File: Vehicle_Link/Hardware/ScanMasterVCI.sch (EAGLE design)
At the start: 86 parts, among them IC1 XMEGA32A4U, IC2 TL331, P1 HARFLEX-1515012-601, Q1 RUM002N05, Q10 ZXMP6A17G, Q3 RUM002N05, Q4 RUM002N05, Q5 RRF015P03, Q6 RUM002N05, Q7 RRF015P03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

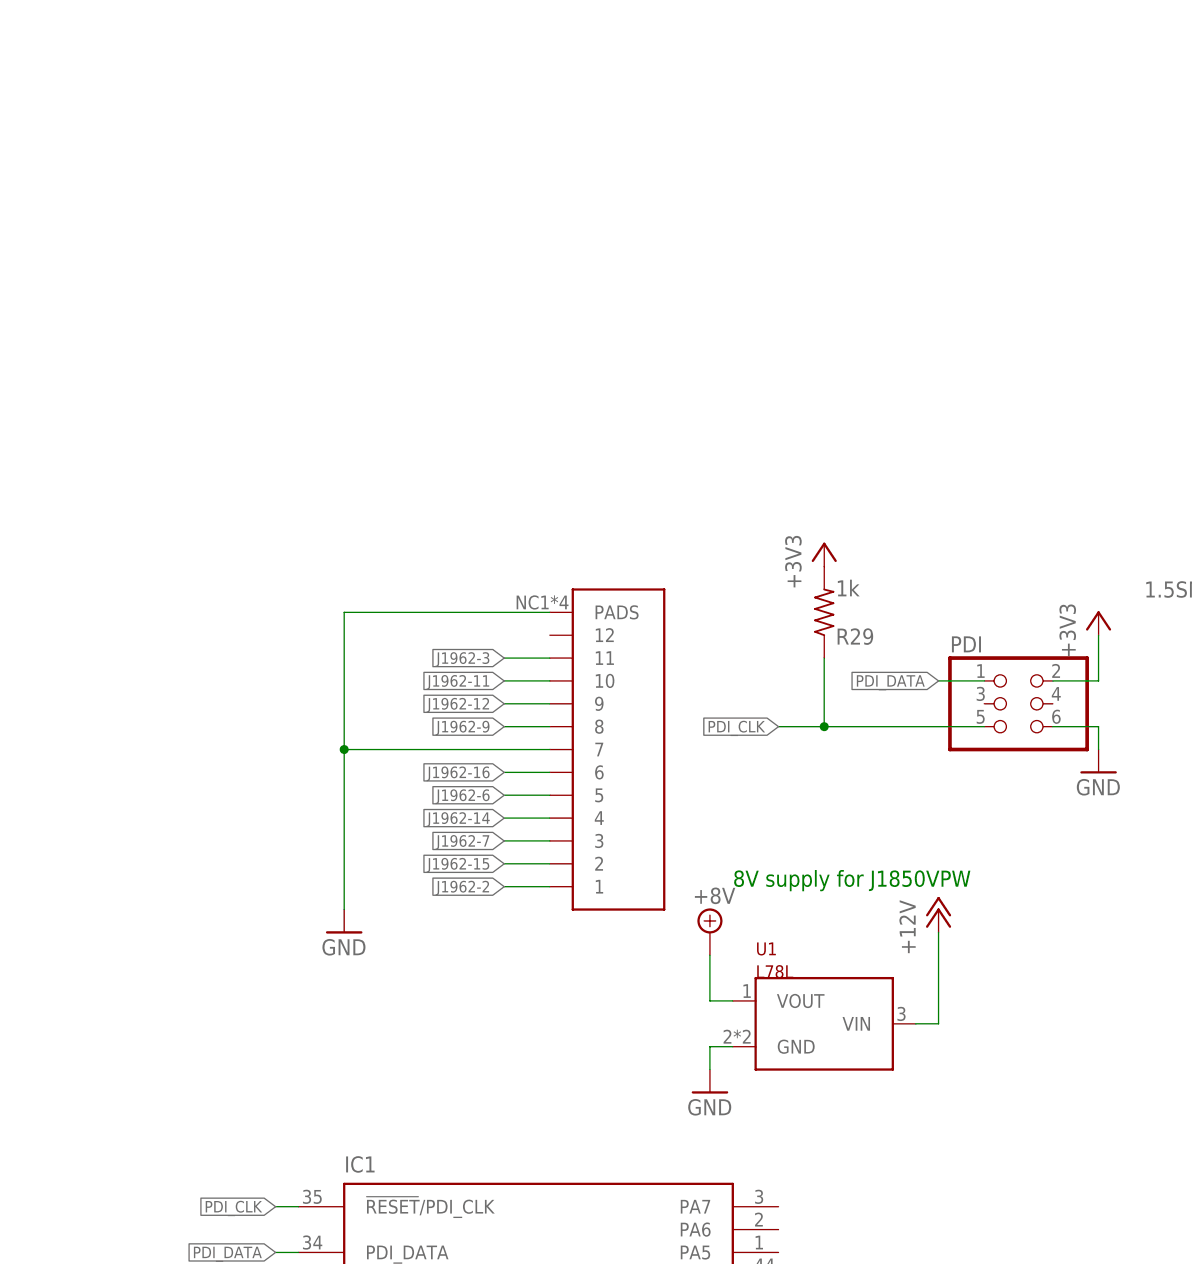
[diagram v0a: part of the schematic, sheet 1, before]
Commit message: Added OBD connector board section, along with proper connectors so I don't have to solder wires anymore. Still need to add milling marks
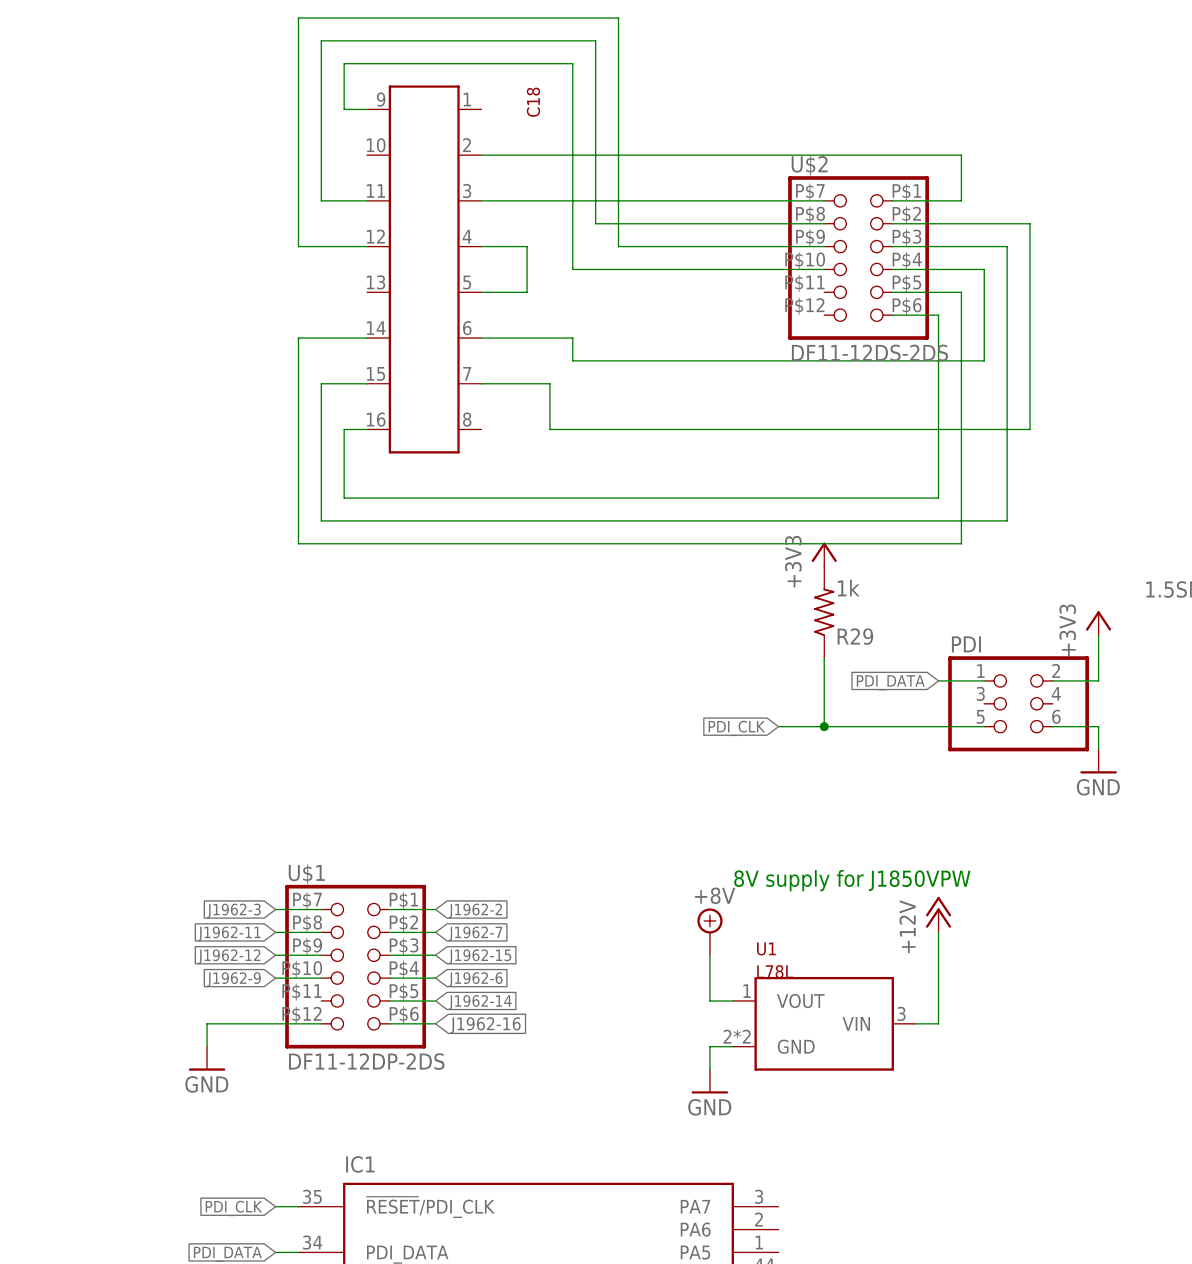
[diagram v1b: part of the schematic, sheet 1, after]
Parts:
- removed P1: HARFLEX-1515012-601, customics:HARFLEX-1515012-601
- added C18: J1962M, customics:J1962M
- added U$1: DF11-12DP-2DS, customics:DF11-12DP-2DS
- added U$2: DF11-12DS-2DS, customics:DF11-12DS-2DS
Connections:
- new net N$14: C18.16, U$2.6
- new net N$25: C18.15, U$2.3
- new net N$28: C18.14, U$2.5
- new net N$29: C18.6, U$2.4
- new net N$32: C18.7, U$2.2
- new net N$40: C18.4, C18.5
- new net N$41: C18.3, U$2.7
- new net N$42: C18.9, U$2.10
- new net N$43: C18.12, U$2.9
- new net N$44: C18.11, U$2.8
- new net N$46: C18.2, U$2.1
- net GND: now also U$1.12; no longer P1.7, P1.PADS
- net J1962-11: now also U$1.8; no longer P1.10
- net J1962-12: now also U$1.9; no longer P1.9
- net J1962-14: now also U$1.5; no longer P1.4
- net J1962-15: now also U$1.3; no longer P1.2
- net J1962-16: now also U$1.6; no longer P1.6
- net J1962-2: now also U$1.1; no longer P1.1
- net J1962-3: now also U$1.7; no longer P1.11
- net J1962-6: now also U$1.4; no longer P1.5
- net J1962-7: now also U$1.2; no longer P1.3
- net J1962-9: now also U$1.10; no longer P1.8

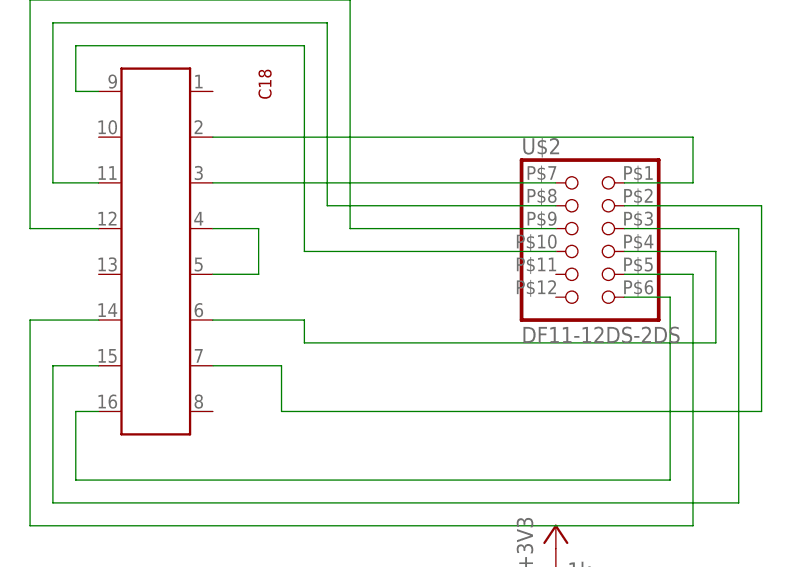
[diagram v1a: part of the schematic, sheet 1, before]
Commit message: Finished adding milling marks to the OBD connector PCB. Missed a ground connection on the OBD board, added it.
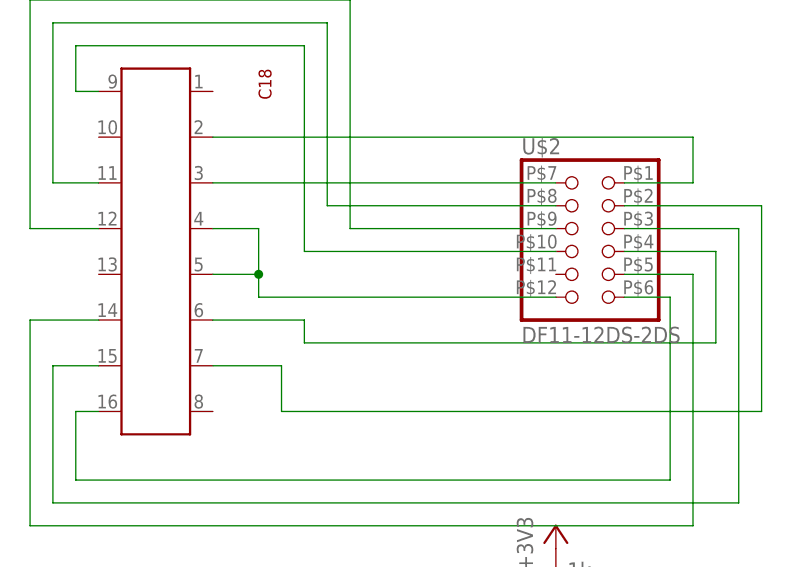
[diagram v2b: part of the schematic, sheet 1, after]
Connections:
- net N$14 renamed CVBATT
- removed net N$40: C18.4, C18.5
- new net CGND: C18.4, C18.5, U$2.12
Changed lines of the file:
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@@
 </segment>
 </net>
-<net name="N$14" class="0">
+<net name="CVBATT" class="1">
 <segment>
 <wire x1="88.9" y1="187.96" x2="88.9" y2="167.64" width="0.1524" layer="91"/>
@@
 </segment>
 </net>
-<net name="N$40" class="0">
+<net name="CGND" class="1">
 <segment>
 <pinref part="C18" gate="G$1" pin="5"/>
@@
 <wire x1="38.1" y1="195.58" x2="43.18" y2="195.58" width="0.1524" layer="91"/>
 <wire x1="43.18" y1="195.58" x2="43.18" y2="190.5" width="0.1524" layer="91"/>
+<wire x1="43.18" y1="190.5" x2="43.18" y2="187.96" width="0.1524" layer="91"/>
+<junction x="43.18" y="190.5"/>
+<pinref part="U$2" gate="G$1" pin="12"/>
+<wire x1="43.18" y1="187.96" x2="76.2" y2="187.96" width="0.1524" layer="91"/>
 </segment>
 </net>

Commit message: Switched XMEGA to the 44QFN variety. Changed the OBD connection, expanded the size of the board just a little to accomodate the new connector.
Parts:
- removed C18: J1962M, customics:J1962M
- removed U$1: DF11-12DP-2DS, customics:DF11-12DP-2DS
- removed U$2: DF11-12DS-2DS, customics:DF11-12DS-2DS
- added OBD1: (no value), customics:OBD2_OBD2_90
- IC1: device atmel:XMEGA16A4A -> atmel:XMEGA16A4M1
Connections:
- removed net CGND: C18.4, C18.5, U$2.12
- removed net CVBATT: C18.16, U$2.6
- removed net N$25: C18.15, U$2.3
- removed net N$28: C18.14, U$2.5
- removed net N$29: C18.6, U$2.4
- removed net N$32: C18.7, U$2.2
- removed net N$41: C18.3, U$2.7
- removed net N$42: C18.9, U$2.10
- removed net N$43: C18.12, U$2.9
- removed net N$44: C18.11, U$2.8
- removed net N$46: C18.2, U$2.1
- net GND: now also OBD1.4, OBD1.5; no longer U$1.12
- net J1962-11: now also OBD1.11; no longer U$1.8
- net J1962-12: now also OBD1.12; no longer U$1.9
- net J1962-14: now also OBD1.14; no longer U$1.5
- net J1962-15: now also OBD1.15; no longer U$1.3
- net J1962-16: now also OBD1.16; no longer U$1.6
- net J1962-2: now also OBD1.2; no longer U$1.1
- net J1962-3: now also OBD1.3; no longer U$1.7
- net J1962-6: now also OBD1.6; no longer U$1.4
- net J1962-7: now also OBD1.7; no longer U$1.2
- net J1962-9: now also OBD1.9; no longer U$1.10
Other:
- moved on the sheet: U3A

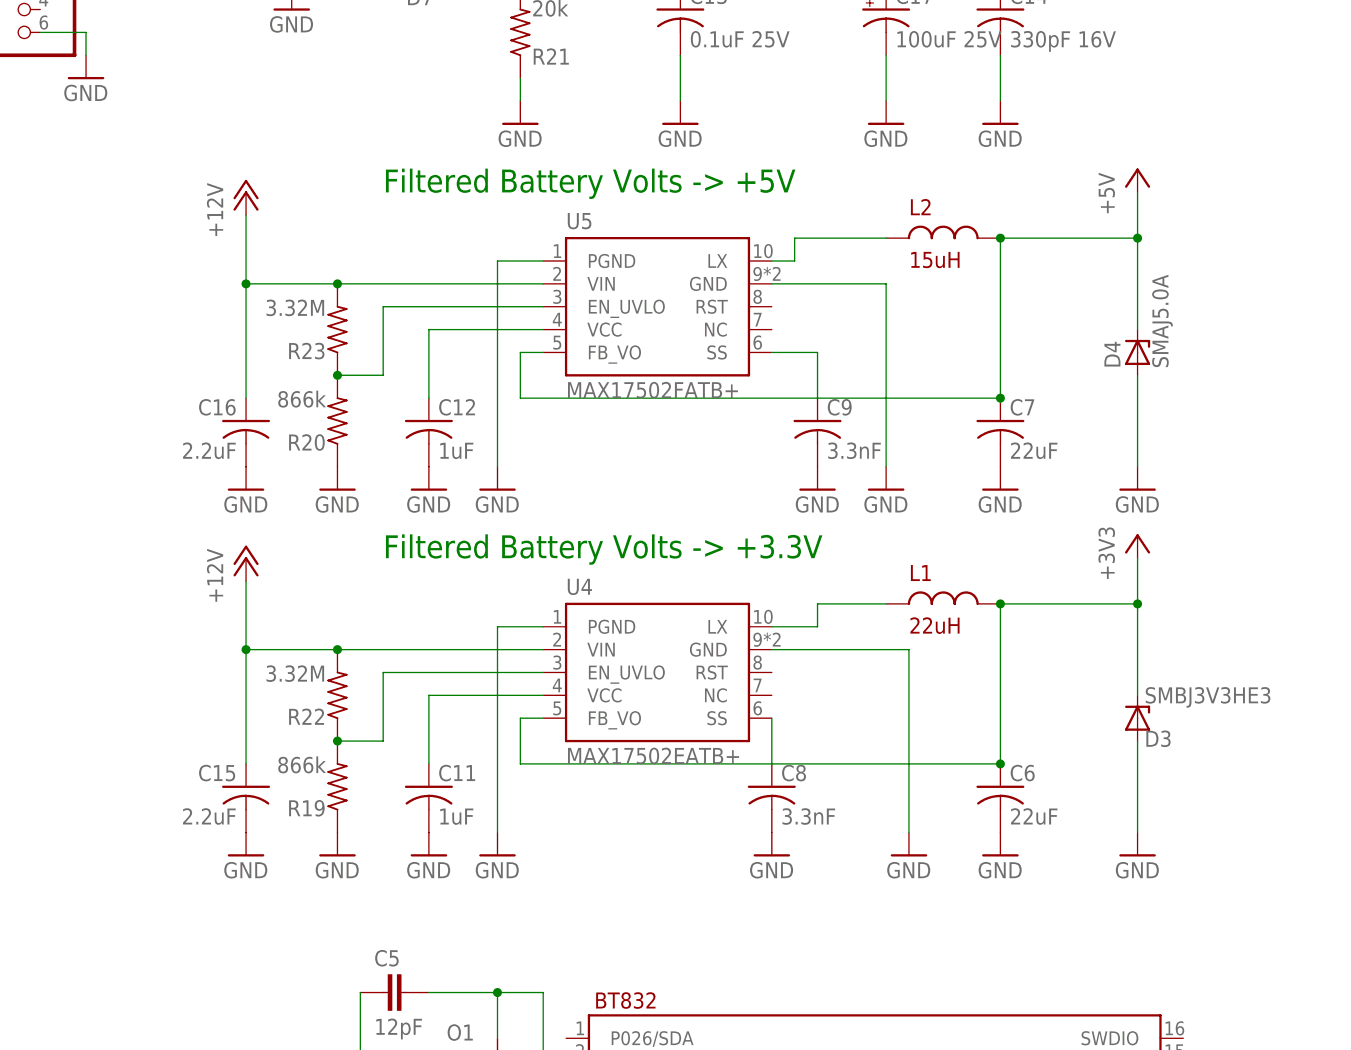
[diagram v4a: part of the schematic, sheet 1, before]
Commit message: Switched voltage ICs to new 600mA chips for easier soldering. Board layout still WIP. Switched XMEGA to be no-lead to save space
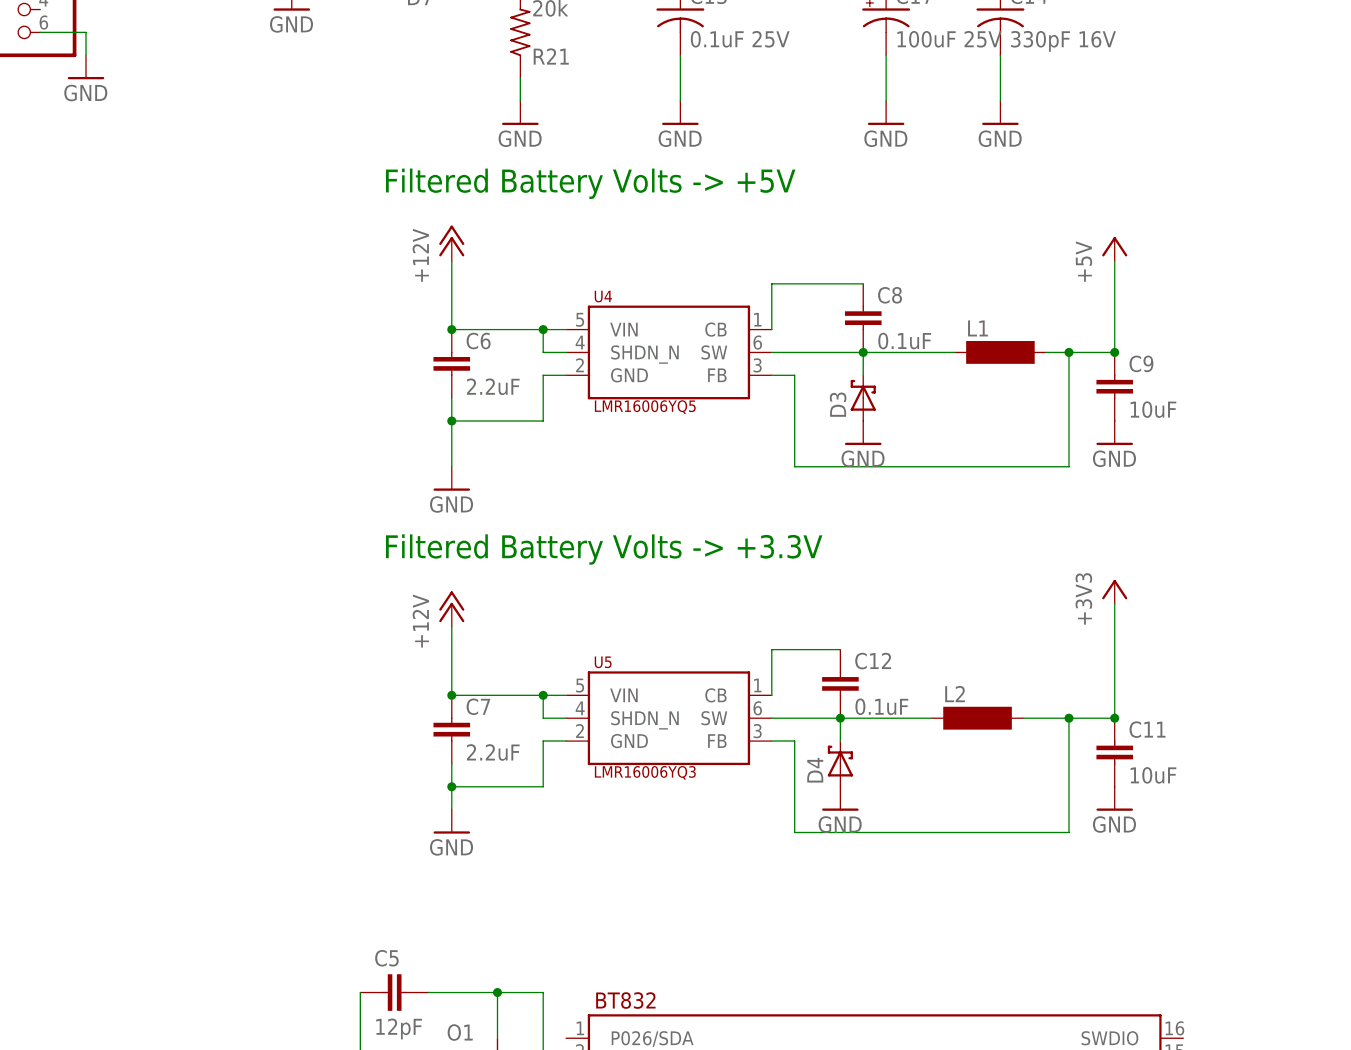
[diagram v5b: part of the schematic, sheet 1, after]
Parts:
- removed C15, C16: 2.2uF, adafruit:C-USC0603
- removed R19, R20: 866k, adafruit:R-US_R0603
- removed R22, R23: 3.32M, adafruit:R-US_R0603
- C11: value 1uF -> 10uF; device adafruit:C-USC0603 -> SparkFun-Capacitors:10UF-0603-6.3V-20%
- C12: value 1uF -> 0.1uF; device adafruit:C-USC0603 -> SparkFun-Capacitors:0.1UF-0603-25V-(+80/-20%)
- C6, C7: value 22uF -> 2.2uF; device adafruit:C-USC0603 -> SparkFun-Capacitors:2.2UF-1206-50V-10%
- C8: value 3.3nF -> 0.1uF; device adafruit:C-USC0603 -> SparkFun-Capacitors:0.1UF-0603-25V-(+80/-20%)
- C9: value 3.3nF -> 10uF; device adafruit:C-USC0603 -> SparkFun-Capacitors:10UF-0603-6.3V-20%
- D3: value SMBJ3V3HE3 -> SM5817PL; device diode:ZENER-DIODESMB -> customics:SM5817PL
- D4: value SMAJ5.0A -> SM5817PL; device diode:ZENER-DIODESMB -> customics:SM5817PL
- L1: value 22uH -> (none); device customics:INDUCTOR -> inductor-neosid:SM-1206
- L2: value 15uH -> (none); device customics:INDUCTOR -> inductor-neosid:SM-1206
- U4: value MAX17502EATB+ -> LMR16006YQ5; device customics:MAX17502 -> customics:LMR16006Y
- U5: value MAX17502FATB+ -> LMR16006YQ3; device customics:MAX17502 -> customics:LMR16006Y
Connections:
- removed net N$15: C12.1, U5.VCC
- removed net N$16: R20.2, R23.1, U5.EN_UVLO
- removed net N$17: C9.1, U5.SS
- removed net N$19: L2.1, U5.LX
- net +12V: now also C6.1, C7.1, U4.SHDN_N, U5.SHDN_N; no longer C15.1, C16.1, R22.2, R23.2
- net +3V3: now also C11.1, L2.2, U5.FB; no longer C6.1, D3.C, L1.2, U4.FB_VO
- net +5V: now also C9.1, L1.2, U4.FB; no longer C7.1, D4.C, L2.2, U5.FB_VO
- net GND: no longer C12.2, C15.2, C16.2, C8.2, R19.1, R20.1, U4.PGND, U5.PGND
- net N$12: now also C12.1, U5.CB; no longer L1.1, U4.LX
- net N$3: now also U4.CB; no longer U4.SS
- net N$7: now also C8.2, D3.C, L1.1, U4.SW; no longer R19.2, R22.1, U4.EN_UVLO
- net N$9: now also C12.2, D4.C, L2.1, U5.SW; no longer C11.1, U4.VCC
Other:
- moved on the sheet: C11, C12, C6, C7, C8, C9
